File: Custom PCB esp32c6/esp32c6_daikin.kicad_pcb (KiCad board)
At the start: 2 copper layers, 40 x 25 mm, 26 parts, among them J2 Conn_01x05, Q1 BSS138PS, U1 TPS562246, U2 XIAO-ESP32-C6

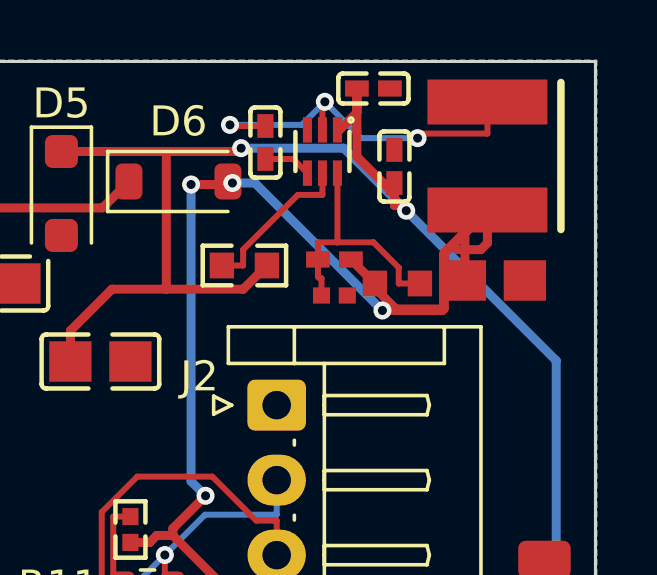
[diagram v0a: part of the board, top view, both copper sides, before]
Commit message: fix(xiao-pcb): FB cluster spacing to real margins + mask-web enforcement
Open the two tightest buck-feedback pad gaps to real v1 margins and turn on
the OSH Park mask-web floor so DRC enforces it.

Item A (copper):
- C19.2<->R6.1 (both /5V_BUCK): 0.100mm -> 0.269mm (target >=0.25).
- R8.2<->R6.1 (GND vs /5V_BUCK): 0.230mm -> 0.480mm (target >=0.30).

R6 is boxed on all four sides (C19 N same-net, R8 W GND, C15 E, and the
5V_BUCK output web S at y94.1). R6-south and C19-north/west both re-seal a
corridor (the 5V_BUCK output web / the VFB sense trace). The clean move is
R6 + C15 east 0.25mm together, shifting the 5V_BUCK output east-wall track
(+0.30) and translating the VFB feed segment east (+0.25) so the VFB divider
geometry and every routed net stay intact. Rejected: R6-south (walls the
5V_BUCK output web to 0.20), C19-west (distorts the VFB sense drop). The
0.25mm move slightly exceeds the 0.1-0.2mm nudge guideline but is the minimum
that clears the fixed 0.10mm same-net corner without re-routing a corridor.
R6/R8/C19 stay tight to U1.6 (VFB); EN/SW routing untouched; both GND pours
re-filled (ZONE_FILLER, single polygon per layer); antenna keep-out copper-free.

Item B: solder_mask_min_width 0 -> 0.1mm (OSH Park web floor) so DRC now
enforces the mask webs Item A opened. solder_mask_bridge = 0 at 0.1mm.

Gates: gating DRC 0/0/0; OSH Park 6-mil method 0/0; smallest different-net
cluster mask web now 0.39mm (was 0.23mm).
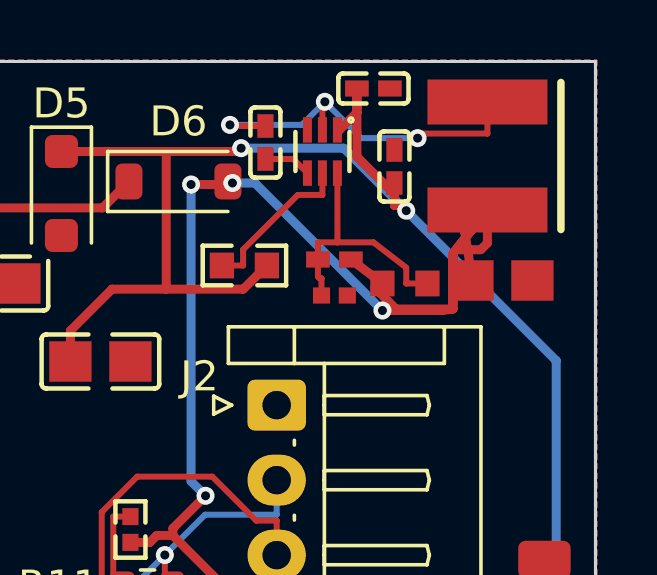
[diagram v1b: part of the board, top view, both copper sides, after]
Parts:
- moved C15 0.25 mm to (186.9, 93.3)
- moved R6 0.25 mm to (183.7, 93.4)
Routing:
- net /5V_BUCK: track 48.9 -> 49.5 mm
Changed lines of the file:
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@@
 		)
 		(pad_to_mask_clearance 0)
+		(solder_mask_min_width 0.1)
 		(allow_soldermask_bridges_in_footprints no)
 		(tenting
@@
 	(footprint "easyeda2kicad:R0603"
 		(layer "F.Cu")
-		(at 183.4 93.4)
+		(at 183.65 93.4)
 		(property "Reference" "R6"
 			(at 0 -4 0)
@@
 	(footprint "easyeda2kicad:C0805"
 		(layer "F.Cu")
-		(at 186.65 93.3)
+		(at 186.9 93.3)
 		(property "Reference" "C15"
 			(at 0 -4 180)
@@
 	)
 	(segment
-		(start 184.95 92.4)
+		(start 185.25 92.4)
 		(end 186.4 90.95)
 		(width 0.3)
@@
 	)
 	(segment
-		(start 182.65 93.4)
+		(start 182.9 93.4)
 		(end 182.65 93.55)
 		(width 0.3)
@@
 	)
 	(segment
-		(start 182.65 93.4)
+		(start 182.9 93.4)
 		(end 181.85 92.6)
 		(width 0.3)
@@
 	)
 	(segment
-		(start 184.95 94.25)
-		(end 184.95 92.4)
+		(start 185.25 94.25)
+		(end 185.25 92.4)
 		(width 0.3)
 		(layer "F.Cu")
@@
 	(segment
 		(start 183.35 94.25)
-		(end 184.95 94.25)
+		(end 185.25 94.25)
 		(width 0.3)
 		(layer "F.Cu")
@@
 	)
 	(segment
-		(start 184.95 94.25)
-		(end 184.95 92.4)
+		(start 185.25 94.25)
+		(end 185.25 92.4)
 		(width 0.3)
 		(layer "F.Cu")
@@
 	(segment
 		(start 184.9 94.3)
-		(end 184.95 94.25)
+		(end 185.25 94.25)
 		(width 0.3)
 		(layer "F.Cu")
@@
 	)
 	(segment
-		(start 184.95 92.4)
+		(start 185.25 92.4)
 		(end 186.4 90.95)
 		(width 0.3)
@@
 	)
 	(segment
-		(start 185.65 93.3)
+		(start 185.9 93.3)
 		(end 185.65 91.7)
 		(width 0.3)
@@
 	(segment
 		(start 182.6016 92.0283)
-		(end 183.4433 92.87)
+		(end 183.6933 92.87)
 		(width 0.2)
 		(layer "F.Cu")
@@
 	)
 	(segment
-		(start 183.4433 92.87)
-		(end 183.4433 93.4)
+		(start 183.6933 92.87)
+		(end 183.6933 93.4)
 		(width 0.2)
 		(layer "F.Cu")
@@
 	)
 	(segment
-		(start 184.15 93.4)
-		(end 183.4433 93.4)
+		(start 184.4 93.4)
+		(end 183.6933 93.4)
 		(width 0.2)
 		(layer "F.Cu")
